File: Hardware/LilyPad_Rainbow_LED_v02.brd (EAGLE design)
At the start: 38.6 x 12.7 mm, 36 parts

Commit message: Updated Board and Schemtic Files
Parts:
- R28, R29, R30, R31, R32, R33, R34: value 180 -> 150
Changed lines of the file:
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@@
 </autorouter>
 <elements>
-<element name="R28" library="SparkFun" package="0603-RES" value="180" x="13.99" y="7.289" smashed="yes" rot="R180">
+<element name="R28" library="SparkFun" package="0603-RES" value="150" x="13.99" y="7.289" smashed="yes" rot="R180">
 <attribute name="NAME" x="14.879" y="6.527" size="1.27" layer="25" font="vector" rot="R180"/>
 <attribute name="VALUE" x="14.498" y="6.781" size="0.4064" layer="27" font="vector" rot="R180"/>
@@
 </element>
 <element name="LOGO29" library="LilyPad-Wearables" package="LOGO-L" value="LOGO-LPL" x="13.97" y="5.1562" rot="MR0"/>
-<element name="R29" library="SparkFun" package="0603-RES" value="180" x="36.342" y="7.289" smashed="yes" rot="R180">
+<element name="R29" library="SparkFun" package="0603-RES" value="150" x="36.342" y="7.289" smashed="yes" rot="R180">
 <attribute name="NAME" x="37.231" y="6.527" size="1.27" layer="25" font="vector" rot="R180"/>
 <attribute name="VALUE" x="36.85" y="6.781" size="0.4064" layer="27" font="vector" rot="R180"/>
@@
 </element>
 <element name="LOGO30" library="LilyPad-Wearables" package="LOGO-L" value="LOGO-LPL" x="36.322" y="5.1562" rot="MR0"/>
-<element name="R30" library="SparkFun" package="0603-RES" value="180" x="30.754" y="7.289" smashed="yes" rot="R180">
+<element name="R30" library="SparkFun" package="0603-RES" value="150" x="30.754" y="7.289" smashed="yes" rot="R180">
 <attribute name="NAME" x="31.643" y="6.527" size="1.27" layer="25" font="vector" rot="R180"/>
 <attribute name="VALUE" x="31.262" y="6.781" size="0.4064" layer="27" font="vector" rot="R180"/>
@@
 </element>
 <element name="LOGO31" library="LilyPad-Wearables" package="LOGO-L" value="LOGO-LPL" x="30.734" y="5.1562" rot="MR0"/>
-<element name="R31" library="SparkFun" package="0603-RES" value="180" x="25.166" y="7.289" smashed="yes" rot="R180">
+<element name="R31" library="SparkFun" package="0603-RES" value="150" x="25.166" y="7.289" smashed="yes" rot="R180">
 <attribute name="NAME" x="26.055" y="6.527" size="1.27" layer="25" font="vector" rot="R180"/>
 <attribute name="VALUE" x="25.674" y="6.781" size="0.4064" layer="27" font="vector" rot="R180"/>
@@
 </element>
 <element name="LOGO32" library="LilyPad-Wearables" package="LOGO-L" value="LOGO-LPL" x="25.146" y="5.1562" rot="MR0"/>
-<element name="R32" library="SparkFun" package="0603-RES" value="180" x="19.578" y="7.289" smashed="yes" rot="R180">
+<element name="R32" library="SparkFun" package="0603-RES" value="150" x="19.578" y="7.289" smashed="yes" rot="R180">
 <attribute name="NAME" x="20.467" y="6.527" size="1.27" layer="25" font="vector" rot="R180"/>
 <attribute name="VALUE" x="20.086" y="6.781" size="0.4064" layer="27" font="vector" rot="R180"/>
@@
 </element>
 <element name="LOGO33" library="LilyPad-Wearables" package="LOGO-L" value="LOGO-LPL" x="19.558" y="5.1562" rot="MR0"/>
-<element name="R33" library="SparkFun" package="0603-RES" value="180" x="8.402" y="7.289" smashed="yes" rot="R180">
+<element name="R33" library="SparkFun" package="0603-RES" value="150" x="8.402" y="7.289" smashed="yes" rot="R180">
 <attribute name="NAME" x="9.291" y="6.527" size="1.27" layer="25" font="vector" rot="R180"/>
 <attribute name="VALUE" x="8.91" y="6.781" size="0.4064" layer="27" font="vector" rot="R180"/>
@@
 </element>
 <element name="LOGO34" library="LilyPad-Wearables" package="LOGO-L" value="LOGO-LPL" x="8.382" y="5.1562" rot="MR0"/>
-<element name="R34" library="SparkFun" package="0603-RES" value="180" x="2.814" y="7.289" smashed="yes" rot="R180">
+<element name="R34" library="SparkFun" package="0603-RES" value="150" x="2.814" y="7.289" smashed="yes" rot="R180">
 <attribute name="NAME" x="3.703" y="6.527" size="1.27" layer="25" font="vector" rot="R180"/>
 <attribute name="VALUE" x="3.322" y="6.781" size="0.4064" layer="27" font="vector" rot="R180"/>

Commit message: updated Board and Schematic files
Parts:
- added E$2: (no value), SparkFun-Aesthetics:REVISION
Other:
- board text added: "0.032" board thickness Purple Silk"
- board text added: "Leah Buechley"

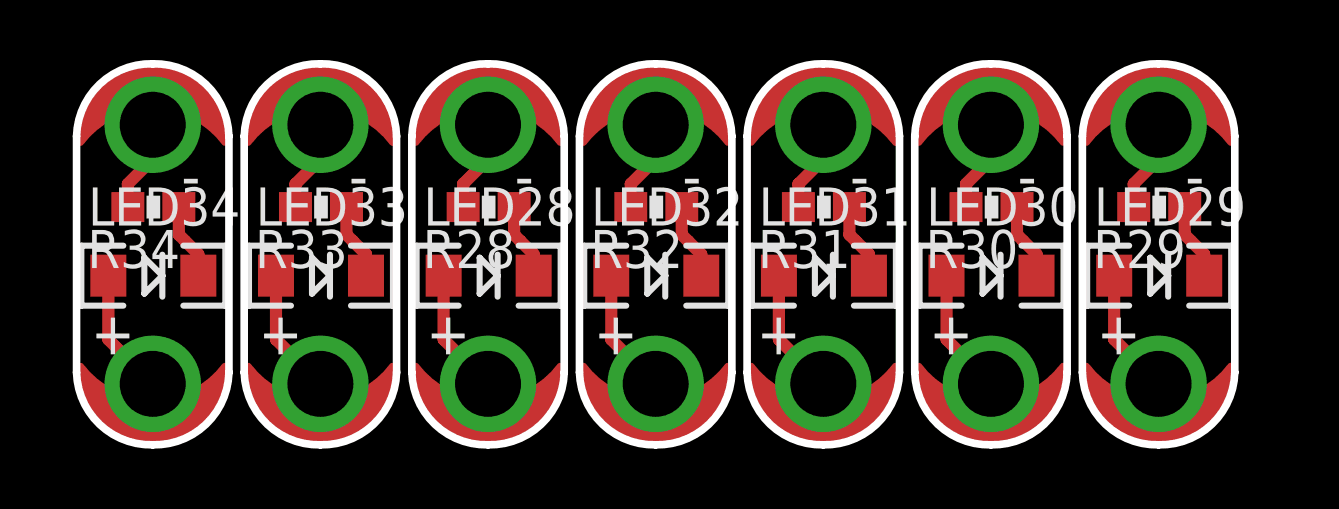
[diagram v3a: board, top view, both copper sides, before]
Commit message: Updated Board File - Corrected SewTap
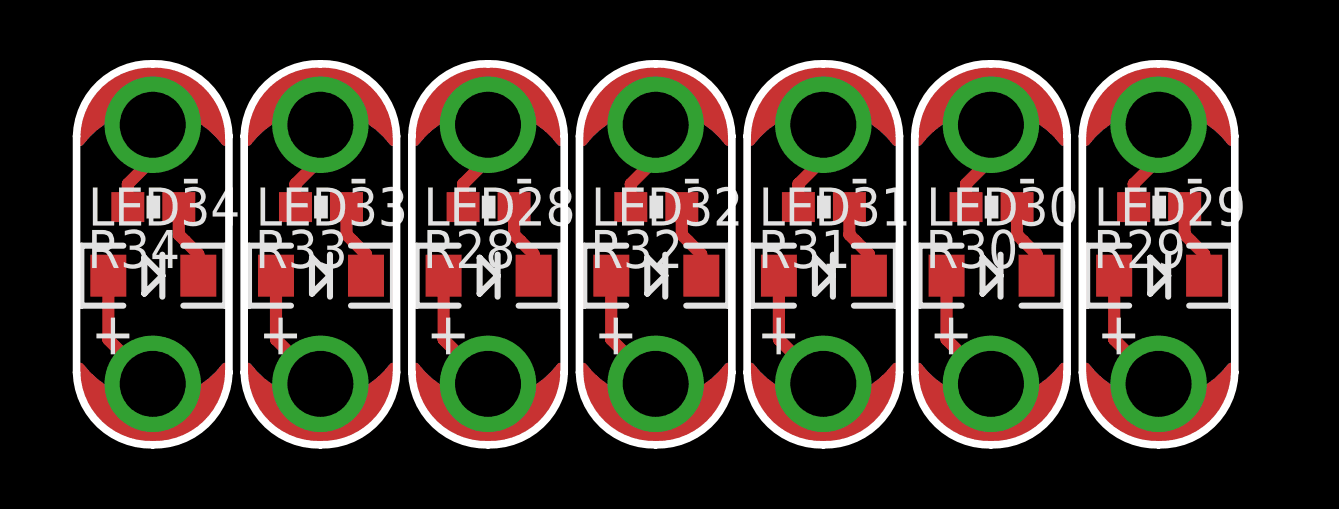
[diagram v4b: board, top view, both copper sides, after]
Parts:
- LED+28, LED+29, LED+30, LED+31, LED+32, LED+33, LED+34, LED-28, LED-29, LED-30, LED-31, LED-32, LED-33, LED-34: device LilyPad-Wearables:PETAL-SMALL -> LilyPad-Wearables:PETAL-SMALL-2SIDE
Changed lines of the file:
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@@
 <setting verticaltext="up"/>
 </settings>
-<grid distance="0.01" unitdist="inch" unit="inch" style="lines" multiple="1" display="yes" altdistance="0.005" altunitdist="inch" altunit="inch"/>
+<grid distance="0.05" unitdist="inch" unit="inch" style="lines" multiple="1" display="yes" altdistance="0.005" altunitdist="inch" altunit="inch"/>
 <layers>
 <layer number="1" name="Top" color="4" fill="1" visible="yes" active="yes"/>
@@
 <attribute name="VALUE" x="14.498" y="6.781" size="0.4064" layer="27" font="vector" rot="R180"/>
 </element>
-<element name="LED+28" library="LilyPad-Wearables" package="PETAL-SMALL" value="SEWTAP6" x="13.97" y="1.397"/>
-<element name="LED-28" library="LilyPad-Wearables" package="PETAL-SMALL" value="SEWTAP6" x="13.97" y="10.033" rot="R180"/>
+<element name="LED+28" library="LilyPad-Wearables" package="PETAL-SMALL-2SIDE" value="SEWTAP6" x="13.97" y="1.397"/>
+<element name="LED-28" library="LilyPad-Wearables" package="PETAL-SMALL-2SIDE" value="SEWTAP6" x="13.97" y="10.033" rot="R180"/>
 <element name="LED28" library="SparkFun-LED" package="LED-1206" value="Red" x="13.99" y="5.003" smashed="yes">
 <attribute name="NAME" x="11.82" y="6.673" size="1.27" layer="25"/>
@@
 <attribute name="VALUE" x="36.85" y="6.781" size="0.4064" layer="27" font="vector" rot="R180"/>
 </element>
-<element name="LED+29" library="LilyPad-Wearables" package="PETAL-SMALL" value="SEWTAP6" x="36.322" y="1.397"/>
-<element name="LED-29" library="LilyPad-Wearables" package="PETAL-SMALL" value="SEWTAP6" x="36.322" y="10.033" rot="R180"/>
+<element name="LED+29" library="LilyPad-Wearables" package="PETAL-SMALL-2SIDE" value="SEWTAP6" x="36.322" y="1.397"/>
+<element name="LED-29" library="LilyPad-Wearables" package="PETAL-SMALL-2SIDE" value="SEWTAP6" x="36.322" y="10.033" rot="R180"/>
 <element name="LED29" library="SparkFun-LED" package="LED-1206" value="White" x="36.342" y="5.003" smashed="yes">
 <attribute name="NAME" x="34.172" y="6.673" size="1.27" layer="25"/>
@@
 <attribute name="VALUE" x="31.262" y="6.781" size="0.4064" layer="27" font="vector" rot="R180"/>
 </element>
-<element name="LED+30" library="LilyPad-Wearables" package="PETAL-SMALL" value="SEWTAP6" x="30.734" y="1.397"/>
-<element name="LED-30" library="LilyPad-Wearables" package="PETAL-SMALL" value="SEWTAP6" x="30.734" y="10.033" rot="R180"/>
+<element name="LED+30" library="LilyPad-Wearables" package="PETAL-SMALL-2SIDE" value="SEWTAP6" x="30.734" y="1.397"/>
+<element name="LED-30" library="LilyPad-Wearables" package="PETAL-SMALL-2SIDE" value="SEWTAP6" x="30.734" y="10.033" rot="R180"/>
 <element name="LED30" library="SparkFun-LED" package="LED-1206" value="Blue" x="30.754" y="5.003" smashed="yes">
 <attribute name="NAME" x="28.584" y="6.673" size="1.27" layer="25"/>
@@
 <attribute name="VALUE" x="25.674" y="6.781" size="0.4064" layer="27" font="vector" rot="R180"/>
 </element>
-<element name="LED+31" library="LilyPad-Wearables" package="PETAL-SMALL" value="SEWTAP6" x="25.146" y="1.397"/>
-<element name="LED-31" library="LilyPad-Wearables" package="PETAL-SMALL" value="SEWTAP6" x="25.146" y="10.033" rot="R180"/>
+<element name="LED+31" library="LilyPad-Wearables" package="PETAL-SMALL-2SIDE" value="SEWTAP6" x="25.146" y="1.397"/>
+<element name="LED-31" library="LilyPad-Wearables" package="PETAL-SMALL-2SIDE" value="SEWTAP6" x="25.146" y="10.033" rot="R180"/>
 <element name="LED31" library="SparkFun-LED" package="LED-1206" value="Green" x="25.166" y="5.003" smashed="yes">
 <attribute name="NAME" x="22.996" y="6.673" size="1.27" layer="25"/>
@@
 <attribute name="VALUE" x="20.086" y="6.781" size="0.4064" layer="27" font="vector" rot="R180"/>
 </element>
-<element name="LED+32" library="LilyPad-Wearables" package="PETAL-SMALL" value="SEWTAP6" x="19.558" y="1.397"/>
-<element name="LED-32" library="LilyPad-Wearables" package="PETAL-SMALL" value="SEWTAP6" x="19.558" y="10.033" rot="R180"/>
+<element name="LED+32" library="LilyPad-Wearables" package="PETAL-SMALL-2SIDE" value="SEWTAP6" x="19.558" y="1.397"/>
+<element name="LED-32" library="LilyPad-Wearables" package="PETAL-SMALL-2SIDE" value="SEWTAP6" x="19.558" y="10.033" rot="R180"/>
 <element name="LED32" library="SparkFun-LED" package="LED-1206" value="Yellow" x="19.578" y="5.003" smashed="yes">
 <attribute name="NAME" x="17.408" y="6.673" size="1.27" layer="25"/>
@@
 <attribute name="VALUE" x="8.91" y="6.781" size="0.4064" layer="27" font="vector" rot="R180"/>
 </element>
-<element name="LED+33" library="LilyPad-Wearables" package="PETAL-SMALL" value="SEWTAP6" x="8.382" y="1.397"/>
-<element name="LED-33" library="LilyPad-Wearables" package="PETAL-SMALL" value="SEWTAP6" x="8.382" y="10.033" rot="R180"/>
+<element name="LED+33" library="LilyPad-Wearables" package="PETAL-SMALL-2SIDE" value="SEWTAP6" x="8.382" y="1.397"/>
+<element name="LED-33" library="LilyPad-Wearables" package="PETAL-SMALL-2SIDE" value="SEWTAP6" x="8.382" y="10.033" rot="R180"/>
 <element name="LED33" library="SparkFun-LED" package="LED-1206" value="Pink" x="8.402" y="5.003" smashed="yes">
 <attribute name="NAME" x="6.232" y="6.673" size="1.27" layer="25"/>
@@
 <attribute name="VALUE" x="3.322" y="6.781" size="0.4064" layer="27" font="vector" rot="R180"/>
 </element>
-<element name="LED+34" library="LilyPad-Wearables" package="PETAL-SMALL" value="SEWTAP6" x="2.794" y="1.397"/>
-<element name="LED-34" library="LilyPad-Wearables" package="PETAL-SMALL" value="SEWTAP6" x="2.794" y="10.033" rot="R180"/>
+<element name="LED+34" library="LilyPad-Wearables" package="PETAL-SMALL-2SIDE" value="SEWTAP6" x="2.794" y="1.397"/>
+<element name="LED-34" library="LilyPad-Wearables" package="PETAL-SMALL-2SIDE" value="SEWTAP6" x="2.794" y="10.033" rot="R180"/>
 <element name="LED34" library="SparkFun-LED" package="LED-1206" value="White" x="2.814" y="5.003" smashed="yes">
 <attribute name="NAME" x="0.644" y="6.673" size="1.27" layer="25"/>

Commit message: Board and Schematic files are Consistent
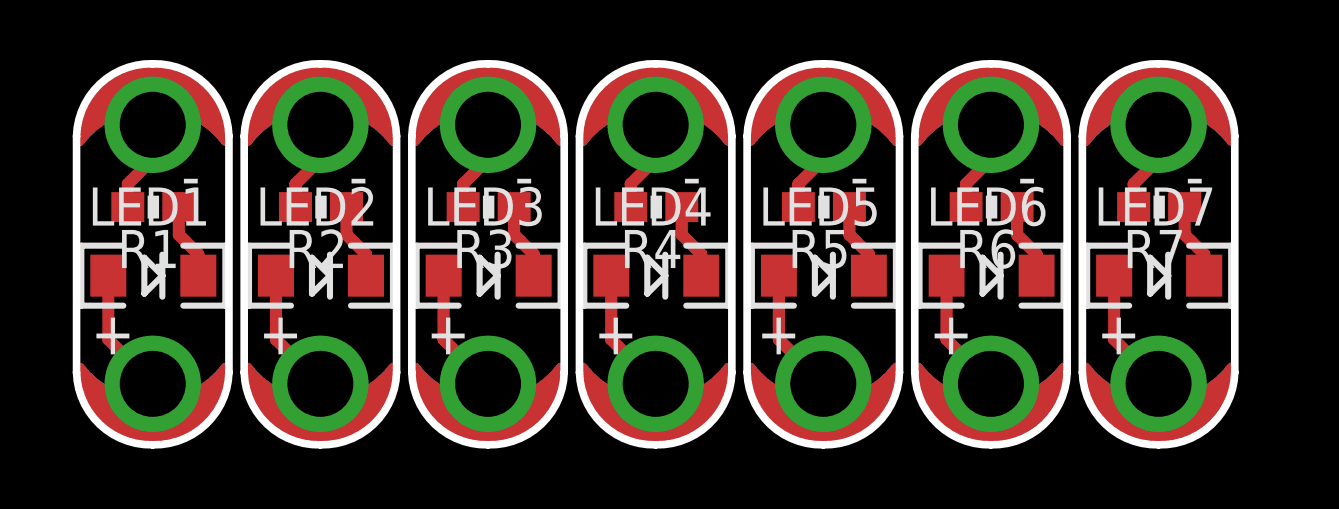
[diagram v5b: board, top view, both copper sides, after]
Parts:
- removed E$1: (no value), SparkFun-Aesthetics:CREATIVE_COMMONS
- removed E$2: (no value), SparkFun-Aesthetics:REVISION
- removed R28, R29, R30, R31, R32, R33, R34: 150, SparkFun:0603-RES
- added R1, R2, R3, R4, R5, R6, R7: 150, SparkFun-Resistors:0603-RES
- LED1, LED7: value White -> WHITE
- LED2: value Pink -> PINK
- LED3: value Red -> RED
- LED4: value Yellow -> YELLOW
- LED5: value Green -> GREEN
- LED6: value Blue -> BLUE
- renumbered LED+28 to LED+3, LED+29 to LED+7, LED+30 to LED+6, LED+31 to LED+5, LED+32 to LED+4, LED+33 to LED+2, LED+34 to LED+1, LED-28 to LED-3, LED-29 to LED-7, LED-30 to LED-6, LED-31 to LED-5, LED-32 to LED-4, LED-33 to LED-2, LED-34 to LED-1, LED28 to LED3, LED29 to LED7, LED30 to LED6, LED31 to LED5, LED32 to LED4, LED33 to LED2, LED34 to LED1
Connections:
- net +28 renamed N$7
- net +29 renamed N$19
- net +30 renamed N$16
- net +31 renamed N$13
- net +32 renamed N$10
- net +33 renamed N$4
- net +34 renamed N$1
- removed net -28: LED-3.1, R28.2
- removed net -29: LED-7.1, R29.2
- removed net -30: LED-6.1, R30.2
- removed net -31: LED-5.1, R31.2
- removed net -32: LED-4.1, R32.2
- removed net -33: LED-2.1, R33.2
- removed net -34: LED-1.1, R34.2
- removed net N$29: LED3.C, R28.1
- removed net N$30: LED7.C, R29.1
- removed net N$31: LED6.C, R30.1
- removed net N$32: LED5.C, R31.1
- removed net N$33: LED4.C, R32.1
- removed net N$34: LED2.C, R33.1
- removed net N$35: LED1.C, R34.1
- new net N$11: LED4.C, R4.1
- new net N$12: LED-4.1, R4.2
- new net N$14: LED5.C, R5.1
- new net N$15: LED-5.1, R5.2
- new net N$17: LED6.C, R6.1
- new net N$18: LED-6.1, R6.2
- new net N$2: LED1.C, R1.1
- new net N$20: LED7.C, R7.1
- new net N$21: LED-7.1, R7.2
- new net N$3: LED-1.1, R1.2
- new net N$5: LED2.C, R2.1
- new net N$6: LED-2.1, R2.2
- new net N$8: LED3.C, R3.1
- new net N$9: LED-3.1, R3.2
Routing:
- net N$21: track 0.00 -> 3.09 mm
- net -29: track 3.09 -> 0.00 mm
- net N$18: track 0.00 -> 3.09 mm
- net N$15: track 0.00 -> 3.09 mm
- net -31: track 3.09 -> 0.00 mm
- net -30: track 3.09 -> 0.00 mm
- net N$9: track 0.00 -> 3.09 mm
- net N$6: track 0.00 -> 3.09 mm
- net N$3: track 0.00 -> 3.09 mm
- net -34: track 3.09 -> 0.00 mm
- net -33: track 3.09 -> 0.00 mm
- net -28: track 3.09 -> 0.00 mm
- net N$12: track 0.00 -> 3.09 mm
- net -32: track 3.09 -> 0.00 mm
- net N$32: track 2.65 -> 0.00 mm
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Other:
- board text removed: "Leah Buechley"
- board text removed: "Mary West"

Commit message: updated Brd and Sch files (in Sync)
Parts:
- added FRAME1: FRAME-LETTER, SparkFun-Aesthetics:CREATIVE_COMMONS
- added U$1: REVISION, SparkFun-Aesthetics:REVISION
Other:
- board text added: "L. Buechley"
- board text added: "M. West"

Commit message: Updated brd file
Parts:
- moved LED+1 34.9 mm to (36.6, 10.0), turned to 180 degrees
- moved LED-1 34.9 mm to (36.6, 1.40), turned to 0 degrees
- moved LED+7 34.4 mm to (3.05, 10.0), turned to 180 degrees
- moved LED-7 34.4 mm to (3.05, 1.40), turned to 0 degrees
- moved R1 33.9 mm to (36.6, 4.14), turned to 0 degrees
- moved LOGO35 33.8 mm to (36.6, 5.44)
- moved LED1 33.8 mm to (36.6, 6.43), turned to 180 degrees
- moved R7 33.5 mm to (3.03, 4.14), turned to 0 degrees
- moved LED7 33.3 mm to (3.03, 6.43), turned to 180 degrees
- moved LOGO30 33.2 mm to (3.12, 5.44)
- moved LED+2 24.2 mm to (31.0, 10.0), turned to 180 degrees
- moved LED-2 24.2 mm to (31.0, 1.40), turned to 0 degrees
- moved LED+6 23.7 mm to (8.64, 10.0), turned to 180 degrees
- moved LED-6 23.7 mm to (8.64, 1.40), turned to 0 degrees
- moved R2 22.8 mm to (31.0, 4.14), turned to 0 degrees
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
